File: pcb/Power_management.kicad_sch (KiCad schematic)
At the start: 24 parts, among them SW2 WAKEUP, U12 LM66100, U13 LM66100, U14 SN74LVC1G14DRL, U15 NCV8165ML330, U16 INA199, U17 MIC94300

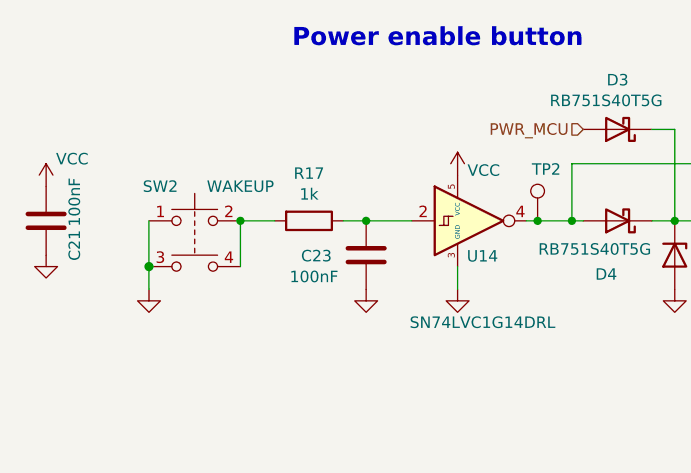
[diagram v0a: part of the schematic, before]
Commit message: Schema & PCB: add pull up to wakeup button
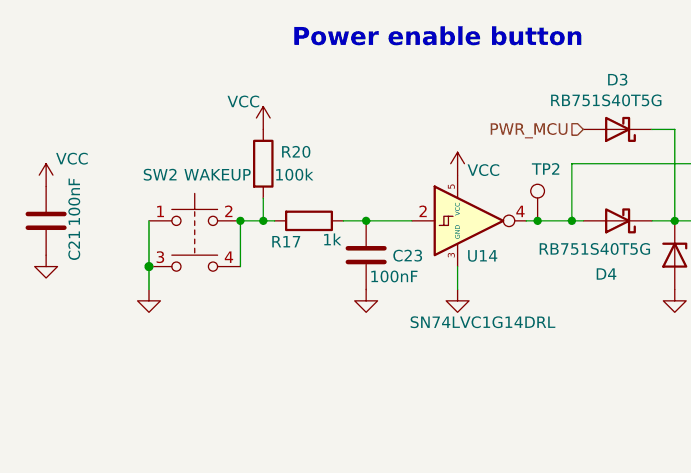
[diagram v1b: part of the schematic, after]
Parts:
- added R20: 100k, Resistor_SMD:R_0603_1608Metric, symbol Device:R
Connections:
- net VCC: now also R20.1
- net at R17.2, SW2.2, SW2.4: now also R20.2
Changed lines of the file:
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@@
   (junction (at 45.72 64.77) (diameter 1.016) (color 0 0 0 0))
   (junction (at 55.88 59.69) (diameter 0.9144) (color 0 0 0 0))
+  (junction (at 58.42 59.69) (diameter 0.9144) (color 0 0 0 0))
   (junction (at 63.5 118.11) (diameter 0.9144) (color 0 0 0 0))
   (junction (at 67.31 118.11) (diameter 0.9144) (color 0 0 0 0))
@@
     (stroke (width 0) (type solid) (color 0 0 0 0))
   )
-  (wire (pts (xy 55.88 59.69) (xy 59.69 59.69))
+  (wire (pts (xy 55.88 59.69) (xy 58.42 59.69))
+    (stroke (width 0) (type solid) (color 0 0 0 0))
+  )
+  (wire (pts (xy 58.42 57.15) (xy 58.42 59.69))
+    (stroke (width 0) (type solid) (color 0 0 0 0))
+  )
+  (wire (pts (xy 58.42 59.69) (xy 59.69 59.69))
     (stroke (width 0) (type solid) (color 0 0 0 0))
   )
@@
     )
   )
+  (symbol (lib_id "power:VCC") (at 58.42 49.53 0) (unit 1)
+    (in_bom yes) (on_board yes)
+    (property "Reference" "#PWR0196" (id 0) (at 58.42 53.34 0)
+      (effects (font (size 1.27 1.27)) hide)
+    )
+    (property "Value" "VCC" (id 1) (at 56.2483 46.4756 0))
+    (property "Footprint" "" (id 2) (at 58.42 49.53 0)
+      (effects (font (size 1.27 1.27)) hide)
+    )
+    (property "Datasheet" "" (id 3) (at 58.42 49.53 0)
+      (effects (font (size 1.27 1.27)) hide)
+    )
+  )
   (symbol (lib_id "power:VCC") (at 63.5 118.11 0) (unit 1)
     (in_bom yes) (on_board yes)
@@
     )
   )
+  (symbol (lib_id "Device:R") (at 58.42 53.34 0) (unit 1)
+    (in_bom yes) (on_board yes)
+    (property "Reference" "R20" (id 0) (at 62.0522 52.07 0))
+    (property "Value" "100k" (id 1) (at 61.824 54.61 0))
+    (property "Footprint" "Resistor_SMD:R_0603_1608Metric" (id 2) (at 56.642 53.34 90)
+      (effects (font (size 1.27 1.27)) hide)
+    )
+    (property "Datasheet" "~" (id 3) (at 58.42 53.34 0)
+      (effects (font (size 1.27 1.27)) hide)
+    )
+  )
   (symbol (lib_id "Device:R") (at 63.5 59.69 270) (unit 1)
     (in_bom yes) (on_board yes)
-    (property "Reference" "R17" (id 0) (at 63.5 54.4322 90))
-    (property "Value" "1k" (id 1) (at 63.5 56.7436 90))
+    (property "Reference" "R17" (id 0) (at 60.96 62.0522 90))
+    (property "Value" "1k" (id 1) (at 66.04 61.8236 90))
     (property "Footprint" "Resistor_SMD:R_0603_1608Metric" (id 2) (at 63.5 57.912 90)
       (effects (font (size 1.27 1.27)) hide)
@@
   (symbol (lib_id "Device:C") (at 69.85 63.5 0) (unit 1)
     (in_bom yes) (on_board yes)
-    (property "Reference" "C23" (id 0) (at 62.611 63.6016 0)
-      (effects (font (size 1.27 1.27)) (justify left))
-    )
-    (property "Value" "100nF" (id 1) (at 61.341 65.913 0)
+    (property "Reference" "C23" (id 0) (at 72.771 63.6016 0)
+      (effects (font (size 1.27 1.27)) (justify left))
+    )
+    (property "Value" "100nF" (id 1) (at 70.231 65.913 0)
       (effects (font (size 1.27 1.27)) (justify left))
     )
@@
   (symbol (lib_id "Switch:SW_Push_Dual") (at 50.8 59.69 0) (unit 1)
     (in_bom yes) (on_board yes)
-    (property "Reference" "SW2" (id 0) (at 46.99 55.88 0))
-    (property "Value" "WAKEUP" (id 1) (at 55.88 55.88 0))
+    (property "Reference" "SW2" (id 0) (at 46.99 54.61 0))
+    (property "Value" "WAKEUP" (id 1) (at 53.34 54.61 0))
     (property "Footprint" "TCY_buttons_switches:EVQ-P7J01P" (id 2) (at 50.8 54.61 0)
       (effects (font (size 1.27 1.27)) hide)

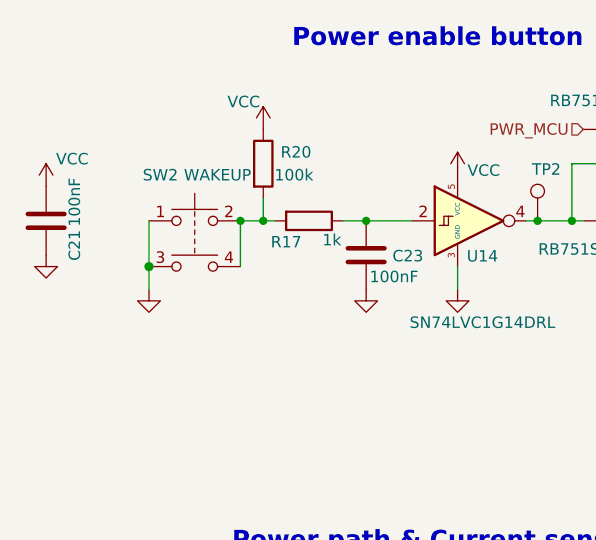
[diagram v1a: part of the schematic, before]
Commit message: PCB: add connection of connector mounting point to ground
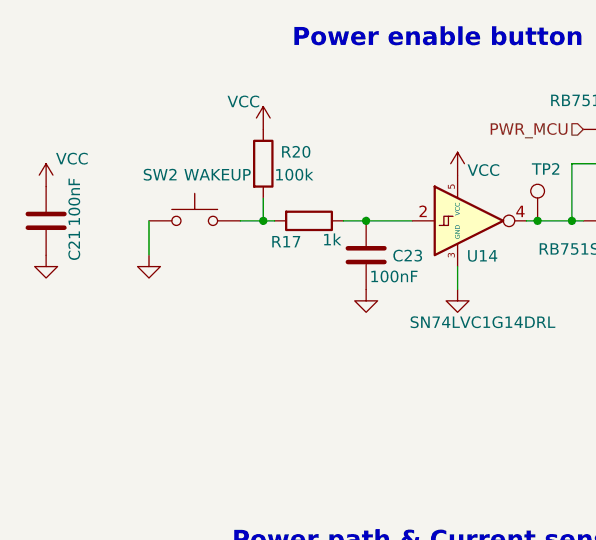
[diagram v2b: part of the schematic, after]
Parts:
- SW2: symbol Switch:SW_Push_Dual -> Switch:SW_Push
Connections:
- net GND: no longer SW2.3
- net at R17.2, R20.2, SW2.2: no longer SW2.4
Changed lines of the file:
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@@
   (junction (at 38.1 132.08) (diameter 0.9144) (color 0 0 0 0))
   (junction (at 41.91 140.97) (diameter 0.9144) (color 0 0 0 0))
-  (junction (at 45.72 64.77) (diameter 1.016) (color 0 0 0 0))
-  (junction (at 55.88 59.69) (diameter 0.9144) (color 0 0 0 0))
   (junction (at 58.42 59.69) (diameter 0.9144) (color 0 0 0 0))
   (junction (at 63.5 118.11) (diameter 0.9144) (color 0 0 0 0))
@@
     (stroke (width 0) (type solid) (color 0 0 0 0))
   )
-  (wire (pts (xy 45.72 59.69) (xy 45.72 64.77))
-    (stroke (width 0) (type solid) (color 0 0 0 0))
-  )
-  (wire (pts (xy 45.72 64.77) (xy 45.72 67.31))
-    (stroke (width 0) (type solid) (color 0 0 0 0))
-  )
-  (wire (pts (xy 55.88 59.69) (xy 55.88 64.77))
+  (wire (pts (xy 45.72 59.69) (xy 45.72 63.5))
     (stroke (width 0) (type solid) (color 0 0 0 0))
   )
@@
     )
   )
-  (symbol (lib_id "power:GND") (at 45.72 67.31 0) (unit 1)
-    (in_bom yes) (on_board yes)
-    (property "Reference" "#PWR0182" (id 0) (at 45.72 73.66 0)
-      (effects (font (size 1.27 1.27)) hide)
-    )
-    (property "Value" "GND" (id 1) (at 49.644 69.094 0)
-      (effects (font (size 1.27 1.27)) hide)
-    )
-    (property "Footprint" "" (id 2) (at 45.72 67.31 0)
-      (effects (font (size 1.27 1.27)) hide)
-    )
-    (property "Datasheet" "" (id 3) (at 45.72 67.31 0)
+  (symbol (lib_id "power:GND") (at 45.72 63.5 0) (unit 1)
+    (in_bom yes) (on_board yes)
+    (property "Reference" "#PWR0182" (id 0) (at 45.72 69.85 0)
+      (effects (font (size 1.27 1.27)) hide)
+    )
+    (property "Value" "GND" (id 1) (at 49.644 65.284 0)
+      (effects (font (size 1.27 1.27)) hide)
+    )
+    (property "Footprint" "" (id 2) (at 45.72 63.5 0)
+      (effects (font (size 1.27 1.27)) hide)
+    )
+    (property "Datasheet" "" (id 3) (at 45.72 63.5 0)
       (effects (font (size 1.27 1.27)) hide)
     )
@@
     )
   )
-  (symbol (lib_id "Switch:SW_Push_Dual") (at 50.8 59.69 0) (unit 1)
+  (symbol (lib_id "Switch:SW_Push") (at 50.8 59.69 0) (unit 1)
     (in_bom yes) (on_board yes)
     (property "Reference" "SW2" (id 0) (at 46.99 54.61 0))

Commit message: Schema & PCB: Update page layout, add notes about SPI modes and I2C addresses
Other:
- company: (none) -> Author: Petr Malaník
- title: (none) -> RingOne
